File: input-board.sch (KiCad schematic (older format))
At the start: 70 parts, among them J1 BTNCON, J12 CAN, J2 BTNCON, J3 SWD, J7 I2C, J8 GAS, J9 BREMSE, SW1 switch-with-led, SW2 switch-with-led, SW3 switch-with-led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

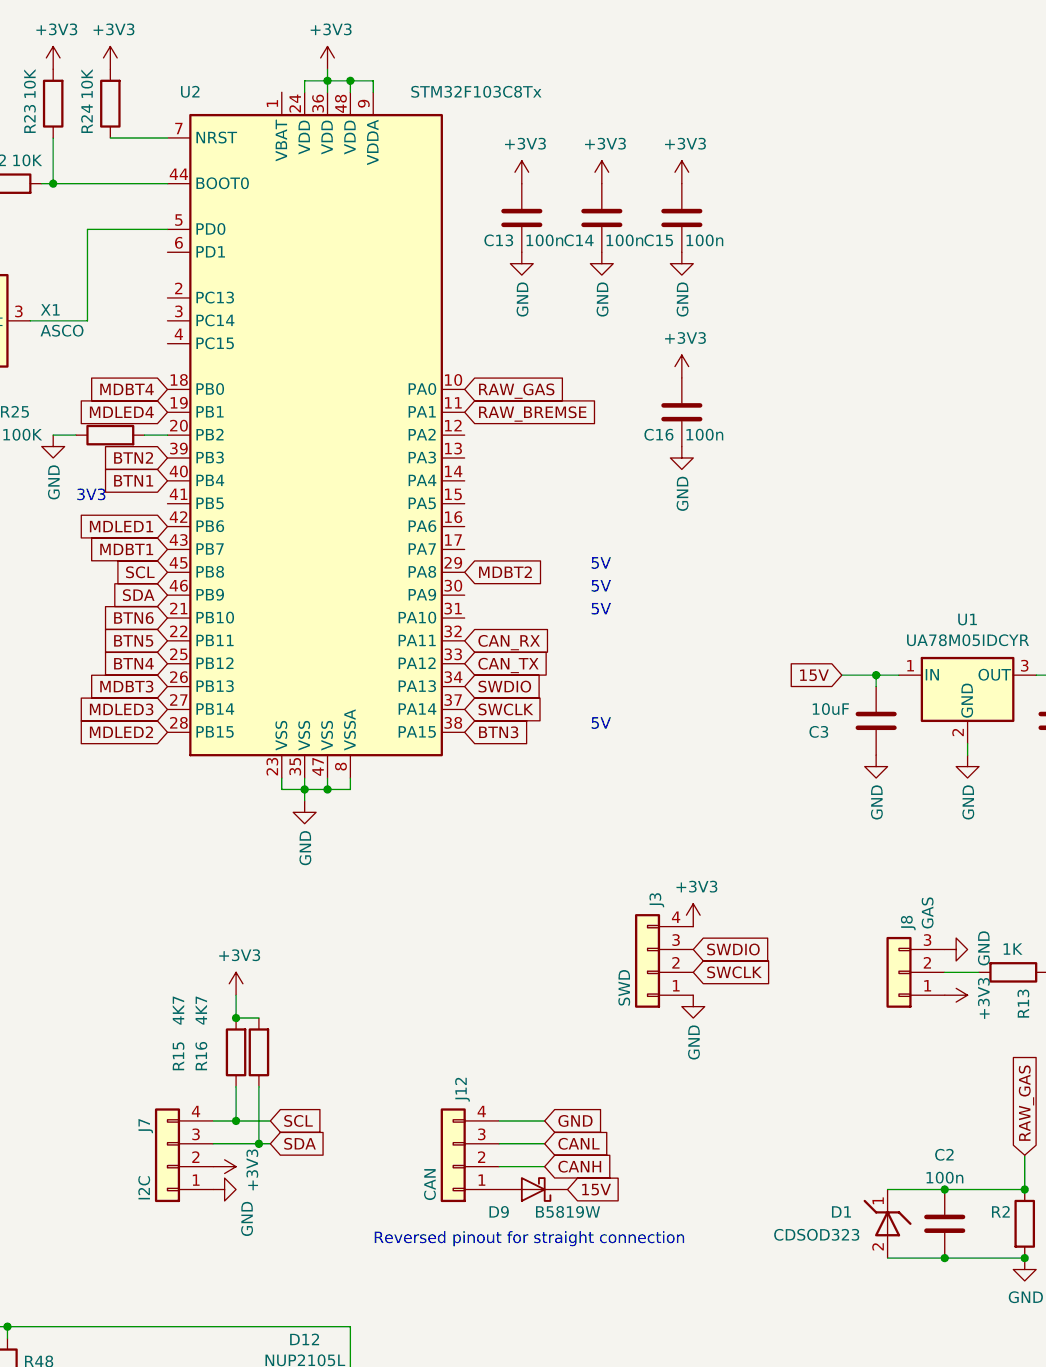
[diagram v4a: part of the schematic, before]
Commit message: Added nc to unused pins
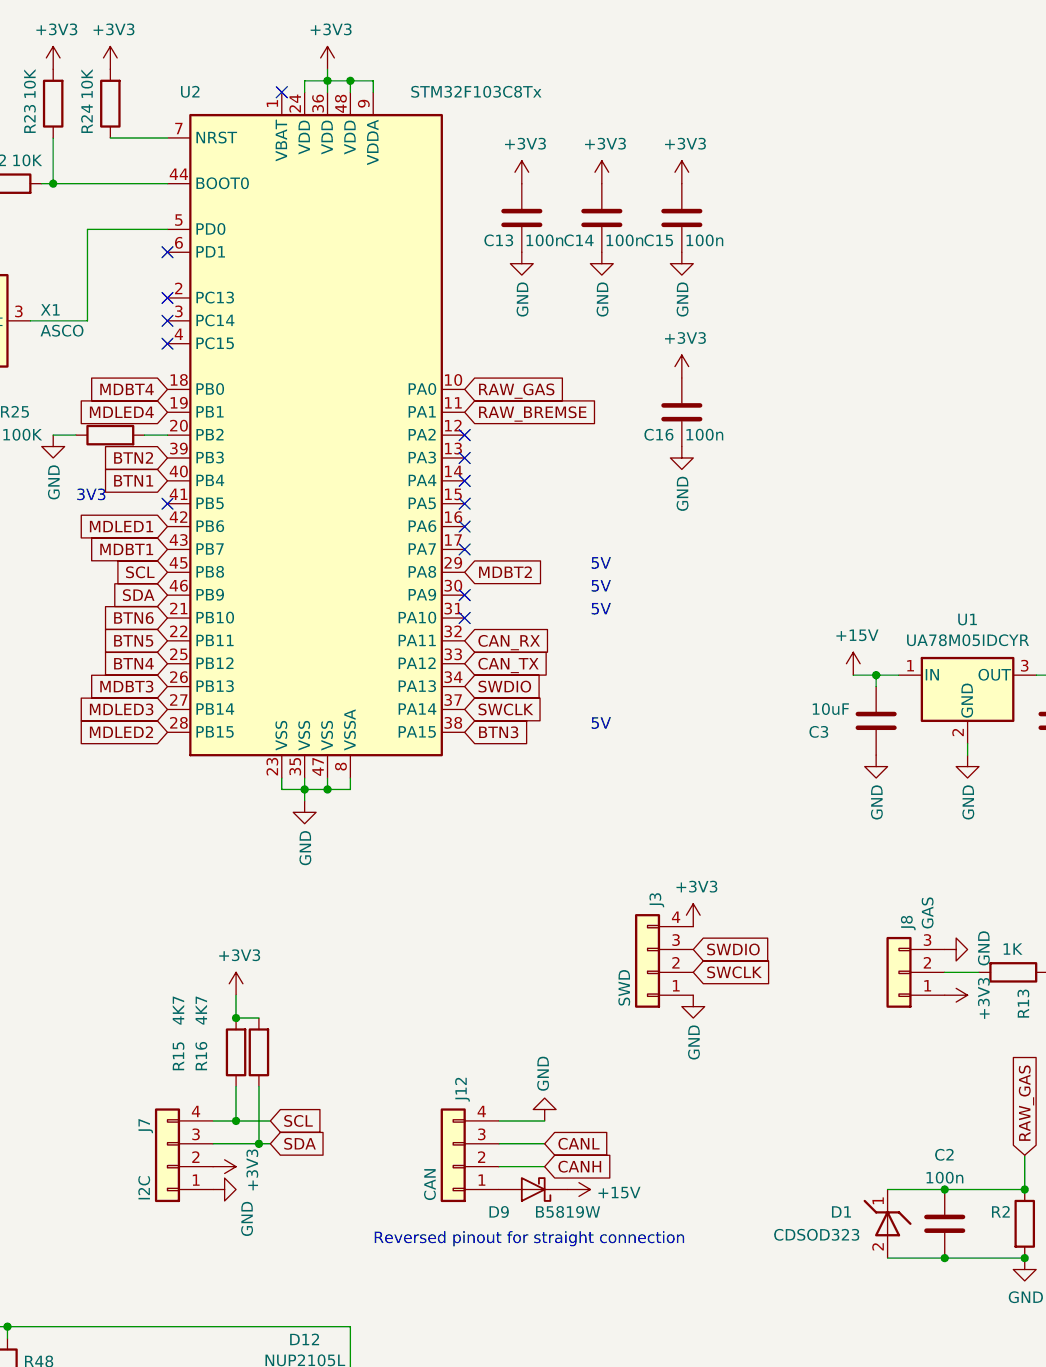
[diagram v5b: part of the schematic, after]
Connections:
- net 15V renamed +15V
- no-connect marks 0 -> 14
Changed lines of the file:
@@
 	0    -1   -1   0
 $EndComp
-$Comp
-L Connector_Generic:Conn_01x03 J8
-U 1 1 5E86CC34
-P 8200 4750
-F 0 "J8" V 8164 4562 50  0000 R CNN
-F 1 "GAS" V 8073 4562 50  0000 R CNN
-F 2 "Connector_PinHeader_2.54mm:PinHeader_1x03_P2.54mm_Horizontal" H 8200 4750 50  0001 C CNN
-F 3 "~" H 8200 4750 50  0001 C CNN
-	1    8200 4750
-	-1   0    0    1
-$EndComp
-Text GLabel 6650 5400 2    50   Input ~ 0
-GND
-Text GLabel 6750 5700 2    50   Input ~ 0
-15V
 Text GLabel 6650 5600 2    50   Input ~ 0
 CANH
@@
 	0    1    1    0
 $EndComp
-Wire Wire Line
-	8550 4750 8400 4750
 Wire Wire Line
 	9650 4750 9850 4750
@@
 	-1   0    0    1
 $EndComp
-Text GLabel 7950 3450 0    50   Input ~ 0
-15V
 $Comp
 L power:GND #PWR03
@@
 $EndComp
 Wire Wire Line
-	7950 3450 8100 3450
-Wire Wire Line
 	8100 3500 8100 3450
 Connection ~ 8100 3450
@@
 Wire Wire Line
 	8500 3800 8500 3750
+$Comp
+L power:GND #PWR0131
+U 1 1 6044F5E3
+P 6650 5400
+F 0 "#PWR0131" H 6650 5150 50  0001 C CNN
+F 1 "GND" V 6655 5272 50  0000 R CNN
+F 2 "" H 6650 5400 50  0001 C CNN
+F 3 "" H 6650 5400 50  0001 C CNN
+	1    6650 5400
+	-1   0    0    1
+$EndComp
+$Comp
+L power:+15V #PWR0132
+U 1 1 6045EA3C
+P 6750 5700
+F 0 "#PWR0132" H 6750 5550 50  0001 C CNN
+F 1 "+15V" V 6765 5828 50  0000 L CNN
+F 2 "" H 6750 5700 50  0001 C CNN
+F 3 "" H 6750 5700 50  0001 C CNN
+	1    6750 5700
+	0    1    1    0
+$EndComp
+$Comp
+L power:+15V #PWR0133
+U 1 1 6046A7D2
+P 8000 3450
+F 0 "#PWR0133" H 8000 3300 50  0001 C CNN
+F 1 "+15V" H 8015 3623 50  0000 C CNN
+F 2 "" H 8000 3450 50  0001 C CNN
+F 3 "" H 8000 3450 50  0001 C CNN
+	1    8000 3450
+	1    0    0    -1
+$EndComp
+Wire Wire Line
+	8000 3450 8100 3450
+NoConn ~ 5000 1800
+NoConn ~ 5000 1900
+NoConn ~ 5000 2000
+NoConn ~ 5000 1600
+NoConn ~ 6300 2400
+NoConn ~ 6300 2500
+NoConn ~ 6300 2600
+NoConn ~ 6300 2700
+NoConn ~ 6300 2800
+NoConn ~ 6300 2900
+NoConn ~ 6300 3100
+NoConn ~ 6300 3200
+NoConn ~ 5000 2700
+Wire Wire Line
+	8550 4750 8400 4750
+$Comp
+L Connector_Generic:Conn_01x03 J8
+U 1 1 5E86CC34
+P 8200 4750
+F 0 "J8" V 8164 4562 50  0000 R CNN
+F 1 "GAS" V 8073 4562 50  0000 R CNN
+F 2 "Connector_PinHeader_2.54mm:PinHeader_1x03_P2.54mm_Horizontal" H 8200 4750 50  0001 C CNN
+F 3 "~" H 8200 4750 50  0001 C CNN
+	1    8200 4750
+	-1   0    0    1
+$EndComp
+NoConn ~ 5500 900
 $EndSCHEMATC

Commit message: Exported manufacturing files Removed backup files
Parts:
- D1, D2, D3, D4, D5, D6, D7, D8: symbol input-board-rescue:CDSOD323-boardcomputer -> input-board:CDSOD323-boardcomputer
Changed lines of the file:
@@
 	5300 4950 5300 4850
 $Comp
-L input-board-rescue:CDSOD323-boardcomputer D1
+L input-board:CDSOD323-boardcomputer D1
 U 1 1 60339500
 P 8150 5800
@@
 	9250 6000 9550 6000
 $Comp
-L input-board-rescue:CDSOD323-boardcomputer D2
+L input-board:CDSOD323-boardcomputer D2
 U 1 1 603375D7
 P 9850 5800
@@
 	2350 2350 2650 2350
 $Comp
-L input-board-rescue:CDSOD323-boardcomputer D4
+L input-board:CDSOD323-boardcomputer D4
 U 1 1 6033E4AF
 P 2650 2150
@@
 	2350 1650 2650 1650
 $Comp
-L input-board-rescue:CDSOD323-boardcomputer D3
+L input-board:CDSOD323-boardcomputer D3
 U 1 1 603C8813
 P 2650 1450
@@
 	3250 4700 3550 4700
 $Comp
-L input-board-rescue:CDSOD323-boardcomputer D7
+L input-board:CDSOD323-boardcomputer D7
 U 1 1 60404627
 P 3550 4500
@@
 	3250 5400 3550 5400
 $Comp
-L input-board-rescue:CDSOD323-boardcomputer D8
+L input-board:CDSOD323-boardcomputer D8
 U 1 1 60404651
 P 3550 5200
@@
 	3250 4000 3550 4000
 $Comp
-L input-board-rescue:CDSOD323-boardcomputer D6
+L input-board:CDSOD323-boardcomputer D6
 U 1 1 6040467B
 P 3550 3800
@@
 $EndComp
 $Comp
-L input-board-rescue:CDSOD323-boardcomputer D5
+L input-board:CDSOD323-boardcomputer D5
 U 1 1 603B76B7
 P 2650 2850
